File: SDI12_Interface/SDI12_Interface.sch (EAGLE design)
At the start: 20 parts, among them J1 CONN_6SCREW_2.54, J2 CONN_32.54_SCREW, U1 SN74LVC1G00SC70, U2 SN74LVC2G241DCU, U3 SN74LVC1G17DCK, U4 MIC5205, U5 LMR62014SOT23

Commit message: Updated part info for SDI12_Interface
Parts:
- C1, C2: value (none) -> 1uF
- C3: value (none) -> 0.1uF
- U4: value MIC5205 -> MIC5205_5V; device bschulz:MIC5205 -> bschulz:MIC5205_5V
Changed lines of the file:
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@@
 <part name="GND2" library="supply1" library_urn="urn:adsk.eagle:library:371" deviceset="GND" device=""/>
 <part name="GND3" library="supply1" library_urn="urn:adsk.eagle:library:371" deviceset="GND" device=""/>
-<part name="U4" library="bschulz" deviceset="MIC5205" device=""/>
-<part name="C1" library="bschulz_passives" deviceset="C-EU" device="C0603" technology="1UF"/>
-<part name="C2" library="bschulz_passives" deviceset="C-EU" device="C0603" technology="1UF"/>
+<part name="U4" library="bschulz" deviceset="MIC5205" device="" technology="_5V" value="MIC5205_5V"/>
+<part name="C1" library="bschulz_passives" deviceset="C-EU" device="C0603" technology="1UF" value="1uF"/>
+<part name="C2" library="bschulz_passives" deviceset="C-EU" device="C0603" technology="1UF" value="1uF"/>
 <part name="GND4" library="supply1" library_urn="urn:adsk.eagle:library:371" deviceset="GND" device=""/>
 <part name="GND9" library="supply1" library_urn="urn:adsk.eagle:library:371" deviceset="GND" device=""/>
-<part name="C3" library="bschulz_passives" deviceset="C-EU" device="C0603" technology="0.1UF"/>
+<part name="C3" library="bschulz_passives" deviceset="C-EU" device="C0603" technology="0.1UF" value="0.1uF"/>
 <part name="GND10" library="supply1" library_urn="urn:adsk.eagle:library:371" deviceset="GND" device=""/>
 <part name="H1" library="bschulz" deviceset="MOUNTING_HOLE" device="2_NP"/>

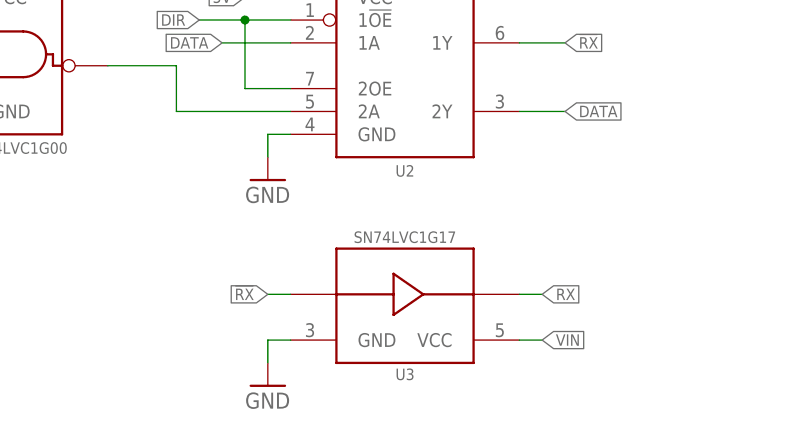
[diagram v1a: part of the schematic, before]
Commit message: Fixed inverter in SDI-12 interface
SDI-12 interface erroneously had non-inverting buffer instead of inverting buffer
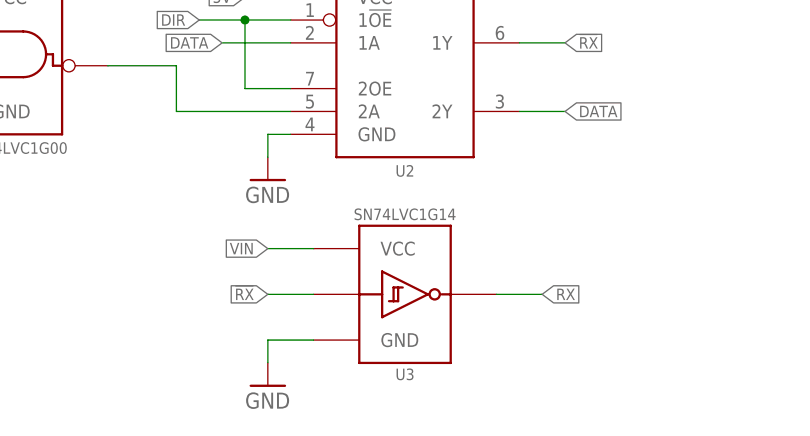
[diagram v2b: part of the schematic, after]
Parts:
- U3: value SN74LVC1G17DCK -> (none); device bschulz:SN74LVC1G17DCK -> bschulz:SN74LVC1G14DCK
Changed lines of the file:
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@@
 <layer number="56" name="wert" color="7" fill="1" visible="no" active="no"/>
 <layer number="57" name="tCAD" color="7" fill="1" visible="no" active="no"/>
+<layer number="58" name="bCAD" color="7" fill="1" visible="no" active="no"/>
 <layer number="59" name="tCarbon" color="7" fill="1" visible="no" active="no"/>
 <layer number="60" name="bCarbon" color="7" fill="1" visible="no" active="no"/>
@@
 <layer number="128" name="_bValues" color="7" fill="1" visible="no" active="yes"/>
 <layer number="129" name="Mask" color="7" fill="1" visible="no" active="yes"/>
+<layer number="130" name="SMDSTROOK" color="7" fill="1" visible="no" active="no"/>
 <layer number="131" name="tAdjust" color="7" fill="1" visible="no" active="yes"/>
 <layer number="132" name="bAdjust" color="7" fill="1" visible="no" active="yes"/>
+<layer number="133" name="bottom_silk" color="7" fill="1" visible="no" active="no"/>
+<layer number="134" name="mbFinish" color="7" fill="1" visible="no" active="no"/>
+<layer number="135" name="mtGlue" color="7" fill="1" visible="no" active="no"/>
+<layer number="136" name="mbGlue" color="7" fill="1" visible="no" active="no"/>
+<layer number="137" name="mtTest" color="7" fill="1" visible="no" active="no"/>
+<layer number="138" name="mbTest" color="7" fill="1" visible="no" active="no"/>
+<layer number="139" name="mtKeepout" color="7" fill="1" visible="no" active="no"/>
+<layer number="140" name="mbKeepout" color="7" fill="1" visible="no" active="no"/>
+<layer number="141" name="mtRestrict" color="7" fill="1" visible="no" active="no"/>
+<layer number="142" name="mbRestrict" color="7" fill="1" visible="no" active="no"/>
+<layer number="143" name="mvRestrict" color="7" fill="1" visible="no" active="no"/>
 <layer number="144" name="Drill_legend" color="7" fill="1" visible="no" active="yes"/>
+<layer number="145" name="mHoles" color="7" fill="1" visible="no" active="no"/>
+<layer number="146" name="mMilling" color="7" fill="1" visible="no" active="no"/>
+<layer number="147" name="mMeasures" color="7" fill="1" visible="no" active="no"/>
+<layer number="148" name="mDocument" color="7" fill="1" visible="no" active="no"/>
+<layer number="149" name="mReference" color="7" fill="1" visible="no" active="no"/>
 <layer number="150" name="Notes" color="7" fill="1" visible="no" active="yes"/>
 <layer number="151" name="HeatSink" color="7" fill="1" visible="no" active="yes"/>
@@
 <layer number="154" name="FabDoc2" color="7" fill="1" visible="no" active="yes"/>
 <layer number="155" name="FabDoc3" color="7" fill="1" visible="no" active="yes"/>
+<layer number="166" name="AntennaArea" color="7" fill="1" visible="no" active="no"/>
+<layer number="168" name="4mmHeightArea" color="7" fill="1" visible="no" active="no"/>
+<layer number="191" name="mNets" color="7" fill="1" visible="no" active="no"/>
+<layer number="192" name="mBusses" color="7" fill="1" visible="no" active="no"/>
+<layer number="193" name="mPins" color="7" fill="1" visible="no" active="no"/>
+<layer number="194" name="mSymbols" color="7" fill="1" visible="no" active="no"/>
+<layer number="195" name="mNames" color="7" fill="1" visible="no" active="no"/>
+<layer number="196" name="mValues" color="7" fill="1" visible="no" active="no"/>
 <layer number="199" name="Contour" color="7" fill="1" visible="no" active="yes"/>
 <layer number="200" name="200bmp" color="7" fill="1" visible="no" active="yes"/>
@@
 <part name="U1" library="bschulz" deviceset="SN74LVC1G00" device="SC70"/>
 <part name="U2" library="bschulz" deviceset="SN74LVC2G241" device="DCU"/>
-<part name="U3" library="bschulz" deviceset="SN74LVC1G17" device="DCK"/>
+<part name="U3" library="bschulz" deviceset="SN74*1G14" device="DCK" technology="LVC"/>
 <part name="J2" library="bschulz" deviceset="CONN_3" device="2.54_SCREW"/>
 <part name="J1" library="bschulz" deviceset="CONN_6" device="SCREW_2.54"/>
@@
 <instance part="U3" gate="G$1" x="68.58" y="25.4" smashed="yes">
 <attribute name="NAME" x="68.58" y="16.51" size="1.27" layer="95" align="center"/>
-<attribute name="DISP" x="68.58" y="31.75" size="1.27" layer="95" ratio="15" align="center"/>
+<attribute name="DISP" x="68.58" y="34.29" size="1.27" layer="95" ratio="15" align="center"/>
 </instance>
 <instance part="J2" gate="G$1" x="7.62" y="104.14" smashed="yes">
@@
 <segment>
 <pinref part="U3" gate="G$1" pin="GND"/>
-<wire x1="55.88" y1="20.32" x2="53.34" y2="20.32" width="0.1524" layer="91"/>
+<wire x1="58.42" y1="20.32" x2="53.34" y2="20.32" width="0.1524" layer="91"/>
 <wire x1="53.34" y1="20.32" x2="53.34" y2="17.78" width="0.1524" layer="91"/>
 <pinref part="GND2" gate="1" pin="GND"/>
@@
 <segment>
 <pinref part="U3" gate="G$1" pin="VCC"/>
-<wire x1="81.28" y1="20.32" x2="83.82" y2="20.32" width="0.1524" layer="91"/>
-<label x="83.82" y="20.32" size="1.27" layer="95" xref="yes"/>
+<wire x1="58.42" y1="30.48" x2="53.34" y2="30.48" width="0.1524" layer="91"/>
+<label x="53.34" y="30.48" size="1.27" layer="95" rot="R180" xref="yes"/>
 </segment>
 <segment>
@@
 <segment>
 <pinref part="U3" gate="G$1" pin="Y"/>
-<wire x1="81.28" y1="25.4" x2="83.82" y2="25.4" width="0.1524" layer="91"/>
+<wire x1="78.74" y1="25.4" x2="83.82" y2="25.4" width="0.1524" layer="91"/>
 <label x="83.82" y="25.4" size="1.27" layer="95" xref="yes"/>
 </segment>
@@
 <segment>
 <pinref part="U3" gate="G$1" pin="A"/>
-<wire x1="55.88" y1="25.4" x2="53.34" y2="25.4" width="0.1524" layer="91"/>
+<wire x1="58.42" y1="25.4" x2="53.34" y2="25.4" width="0.1524" layer="91"/>
 <label x="53.34" y="25.4" size="1.27" layer="95" rot="R180" xref="yes"/>
 </segment>
